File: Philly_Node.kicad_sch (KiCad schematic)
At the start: 72 parts, among them J1 *, J2 LED, J4 USB_C_Receptacle_USB2.0, J5 Multi, Q1 Q_Dual_NMOS_G1S2G2D2S1D1, Q4 Q_NMOS_GSD, SW2 D0, U1 BQ25176JDSGR, U2 MDBT50Q-U1MV2, U3 E22-900M22S, U4 TPS2120YFPR, U5 TPS25200DRVT, Y1 32.768KHz

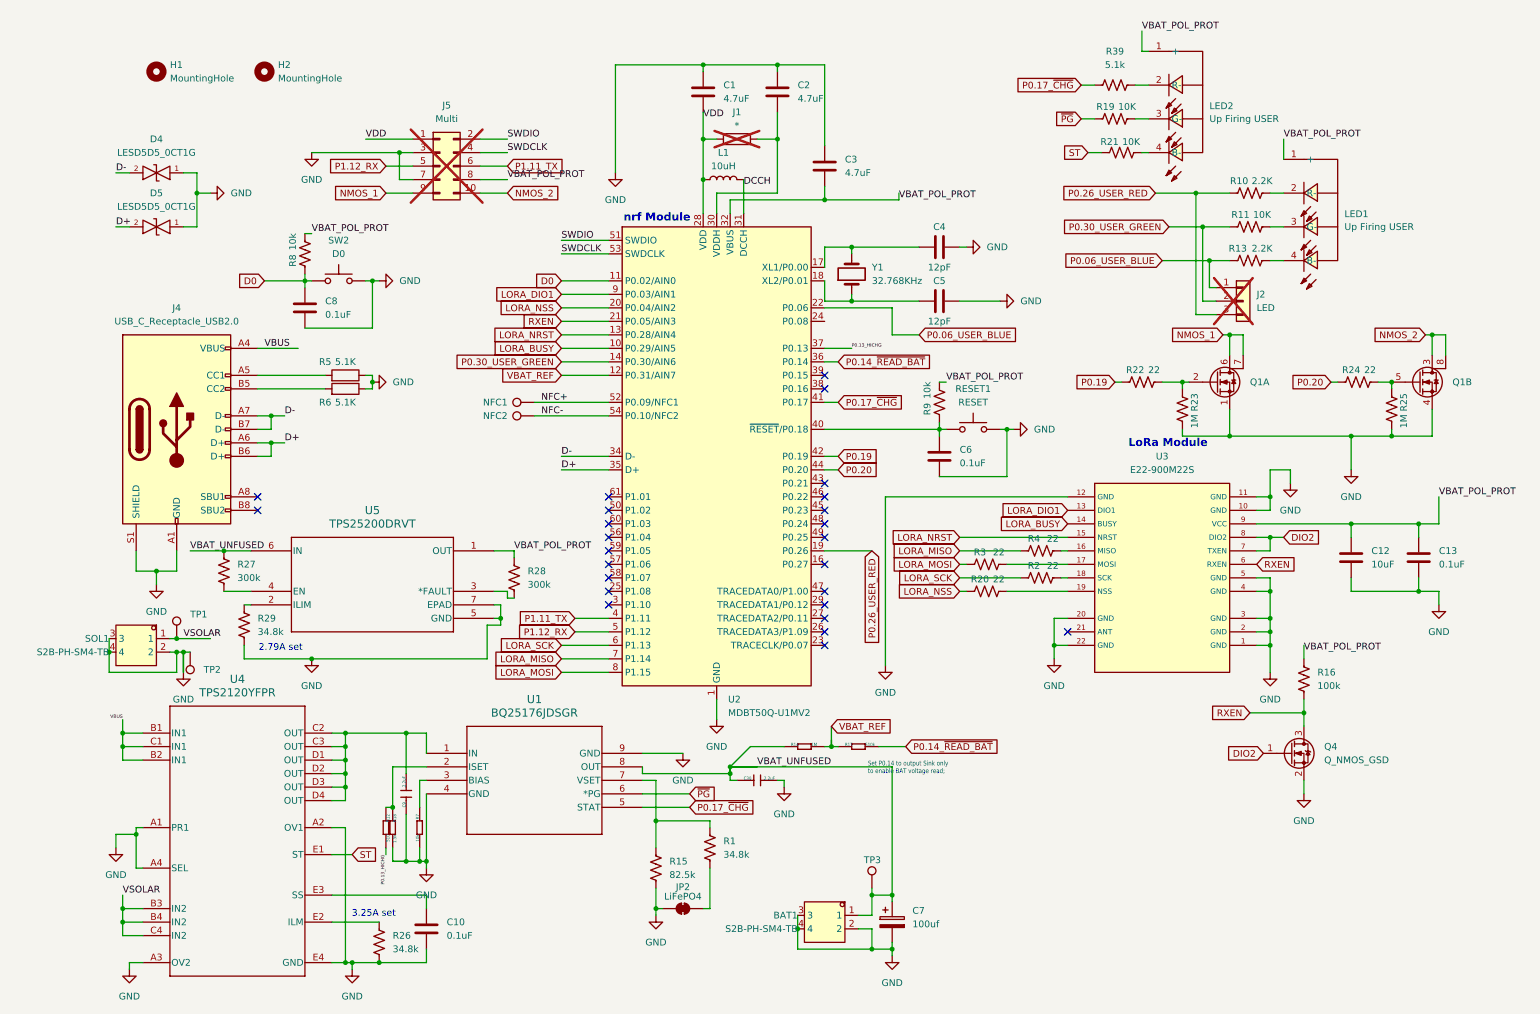
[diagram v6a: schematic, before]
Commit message: Adjustments to routing, added in more signals for solar input detection.
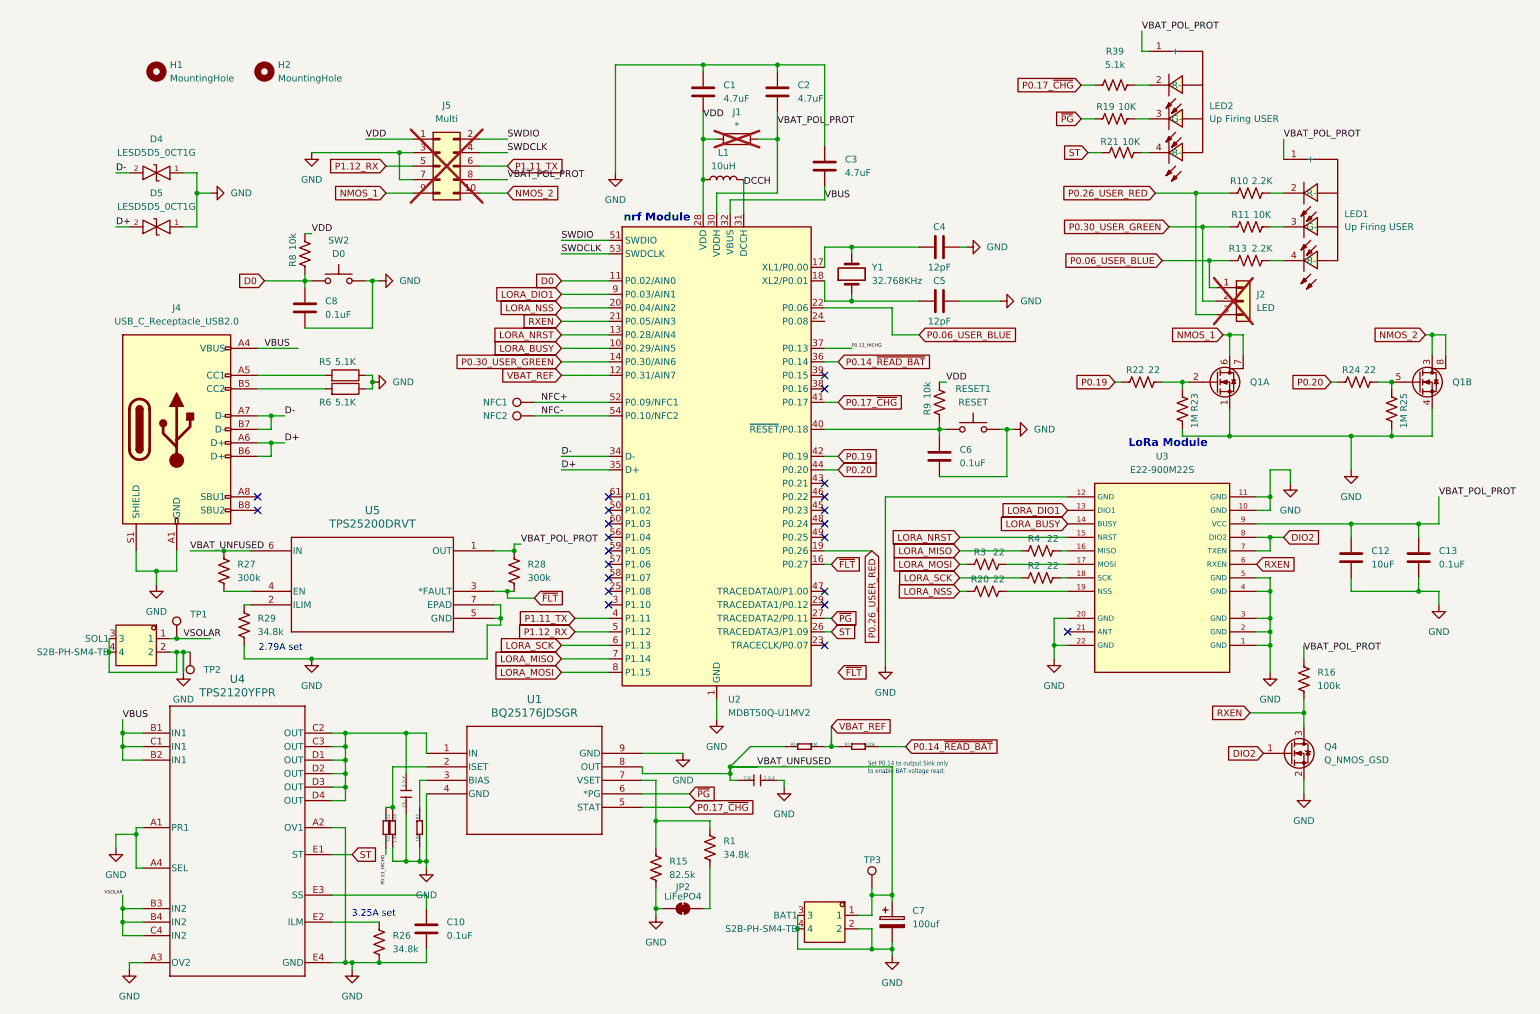
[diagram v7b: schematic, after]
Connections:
- net ST: now also U2.26 (TRACEDATA3/P1.09)
- net VBAT_POL_PROT: now also C2.2, J1.2, U2.30 (VDDH); no longer C3.2, R8.2, R9.2, U2.32 (VBUS)
- net VBUS: now also C3.2, U2.32 (VBUS)
- net VDD: now also R8.2, R9.2
- net ~{PG}: now also U2.27 (TRACEDATA2/P0.11)
- net ~{FLT}: now reaches U2.16 (P0.27)
- net ~{FLT}: now also R28.2, U5.3 (*FAULT)
- no-connect marks 25 -> 22
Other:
- moved on the sheet: R28

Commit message: Add 2 user inputs with ESD diodes, break out old analog battery voltage monitor pin.
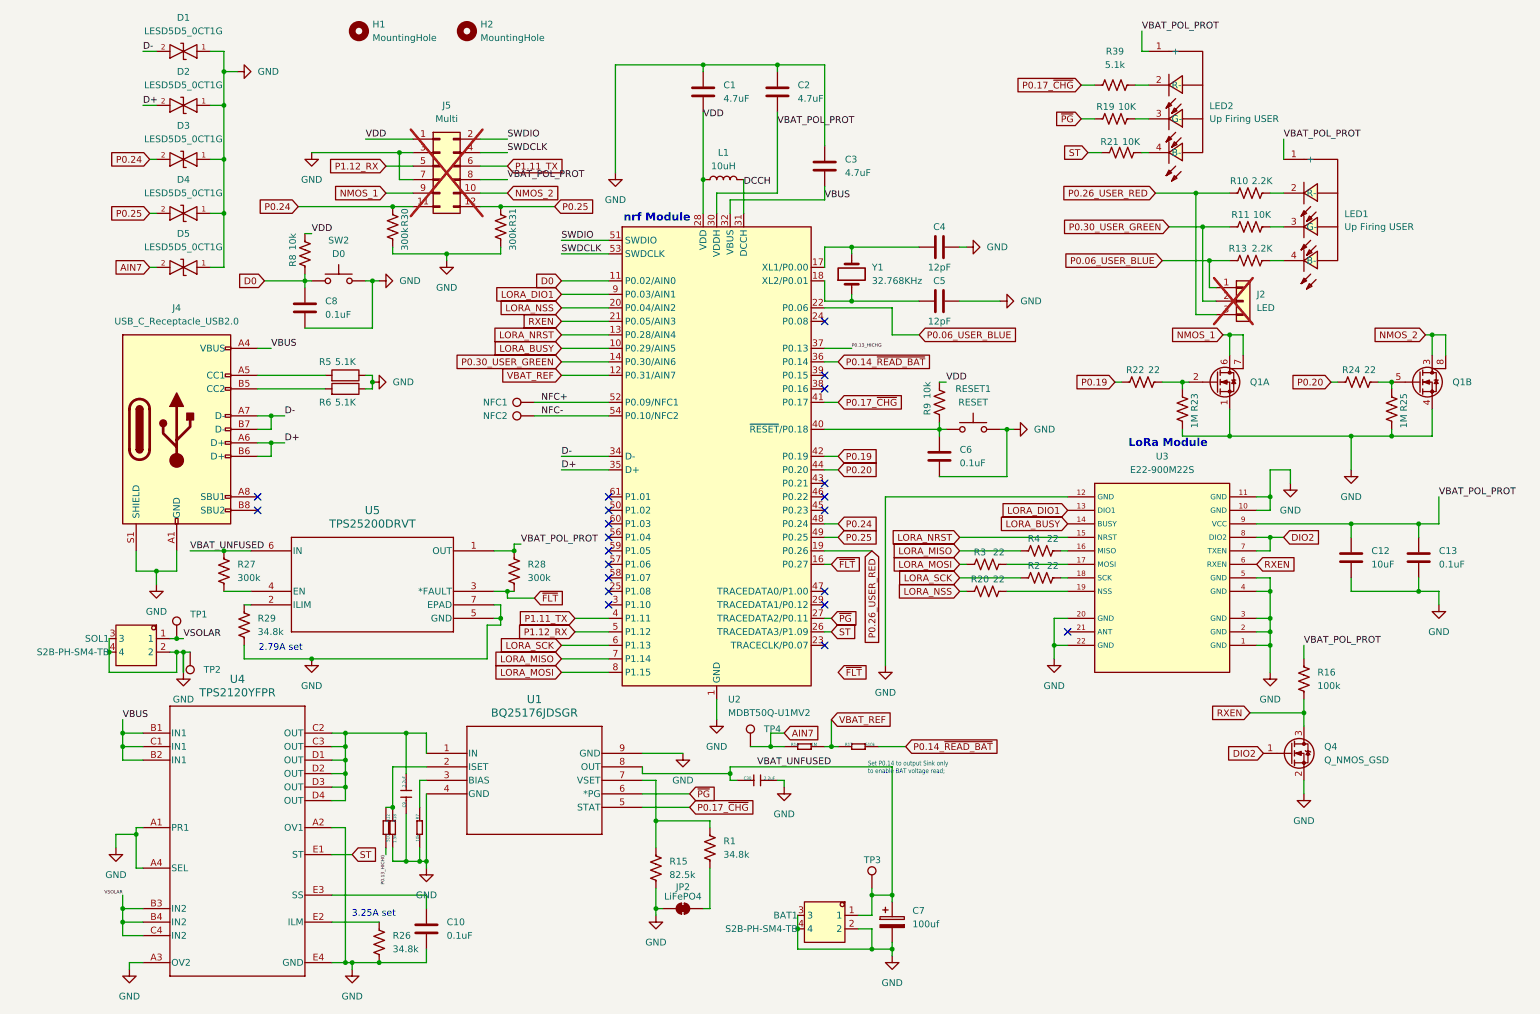
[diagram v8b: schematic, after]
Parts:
- removed J1: *, Philly_Lib:R_0402_1005Metric, symbol Philly_Lib:R
- added D3, D4, D5: LESD5D5_0CT1G, Philly_Lib:SOD-523_L1.2-W0.8-LS1.6-BI, symbol Philly_Lib:LESD5D5_0CT1G
- added R30, R31: 300k, Philly_Lib:R_0402_1005Metric, symbol Philly_Lib:R_US
- added TP4: TestPoint, Philly_Lib:TestPoint_Pad_1.0x1.0mm, symbol Philly_Lib:TestPoint
- J5: footprint Philly_Lib:PinHeader_1x10_P1.27mm_Vertical -> Connector_PinHeader_1.27mm:PinHeader_1x12_P1.27mm_Vertical; symbol Philly_Lib:Conn_02x05_Odd_Even -> Connector_Generic:Conn_02x06_Odd_Even
- renumbered D4 to D1, D5 to D2
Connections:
- net GND: now also D3.1, D4.1, D5.1, R30.2, R31.2
- net VBAT_UNFUSED: no longer R14.1
- net P0.24: now reaches U2.48 (P0.24)
- net P0.24: now also J5.11 (Pin_11), D3.2, R30.1
- net P0.25: now reaches U2.49 (P0.25)
- net P0.25: now also J5.12 (Pin_12), D4.2, R31.1
- new net AIN7: D5.2, R14.1, TP4.1
- no-connect marks 22 -> 21
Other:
- moved on the sheet: D1, D2, H1, H2
